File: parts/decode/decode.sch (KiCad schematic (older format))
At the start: 37 parts, among them J1 Conn_02x02_Odd_Even, J10 Conn_01x02, J11 Conn_01x02, J12 Conn_01x02, J13 Conn_01x02, J14 Conn_02x04_Odd_Even, J2 Conn_02x04_Odd_Even, J3 Conn_01x02, J4 Conn_01x02, J5 Conn_01x02, J6 Conn_01x02, J7 Conn_01x02, J8 Conn_01x02, J9 Conn_01x02, K1 HK19F, K10 HK19F, K11 HK19F, K2 HK19F, K3 HK19F, K4 HK19F, K5 HK19F, K6 HK19F, K7 HK19F, K8 HK19F, K9 HK19F

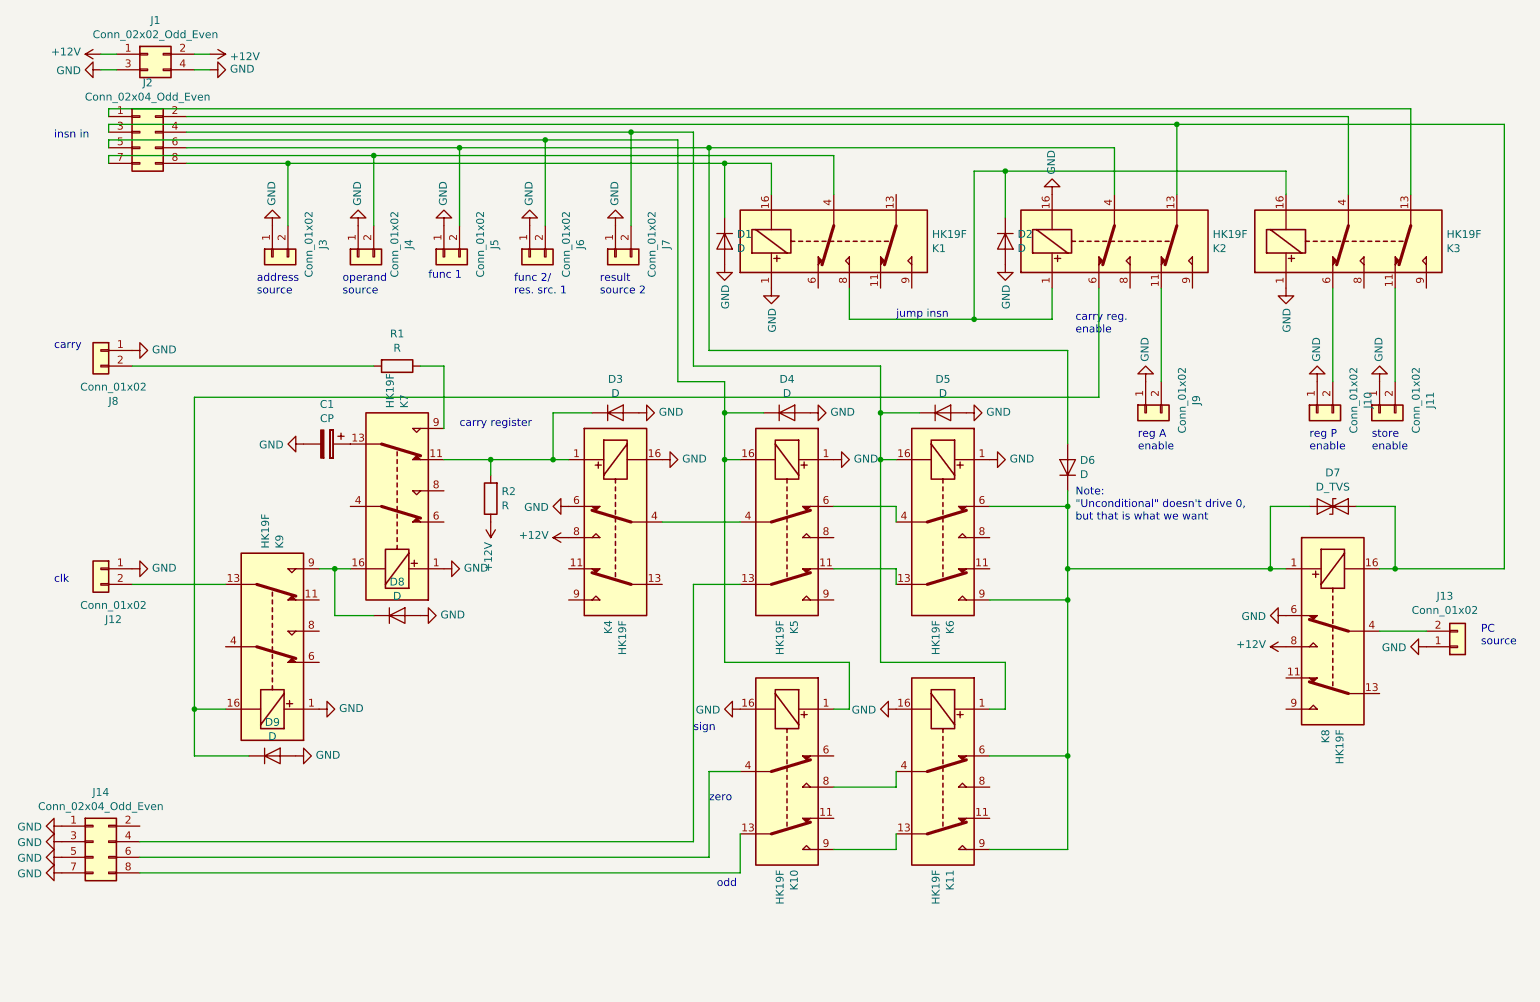
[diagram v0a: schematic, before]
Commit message: Change opcodes (jumps from rediscovered notes).
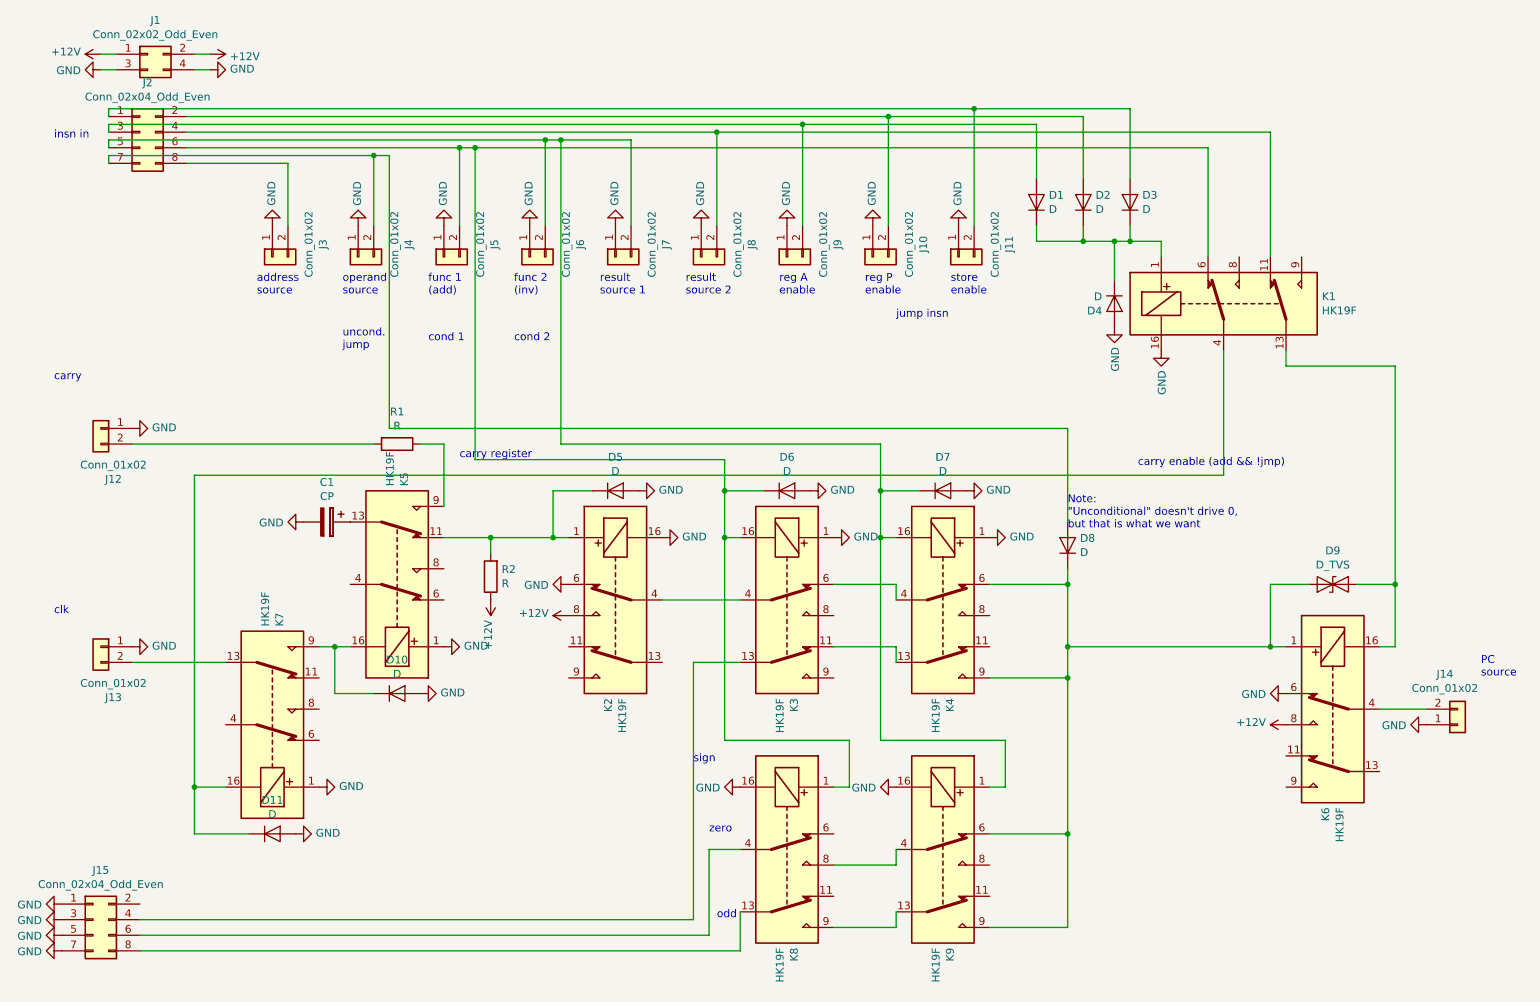
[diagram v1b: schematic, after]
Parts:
- removed K2, K3: HK19F, hk19f:Relay_DPDT_HK19F, symbol hk19f:HK19F
- added D3, D4: D, Diodes_SMD:D_2114, symbol Device:D
- added J7: Conn_01x02, Pin_Headers:Pin_Header_Straight_1x02_Pitch2.54mm, symbol Connector_Generic:Conn_01x02
- renumbered D8 to D10, D9 to D11, D3 to D5, D4 to D6, D5 to D7, D6 to D8, D7 to D9, J8 to J12, J12 to J13, J13 to J14, J14 to J15, J7 to J8, K4 to K2, K5 to K3, K6 to K4, K7 to K5, K8 to K6, K9 to K7, K10 to K8, K11 to K9
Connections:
- net GND: now also K1.16, D4.2 (A), J7.1 (Pin_1); no longer D1.2 (A), D2.2 (A), K1.1
- net at J2.1 (Pin_1): now also J11.2 (Pin_2), D3.2 (A)
- net at J2.2 (Pin_2): now also D2.2 (A), J10.2 (Pin_2)
- net at D9.2 (A2), K6.16: now also K1.13; no longer J2.3 (Pin_3)
- net at D7.1 (K), K4.16, K9.1: now also J2.5 (Pin_5), J6.2 (Pin_2), J7.2 (Pin_2); no longer J2.4 (Pin_4), J8.2 (Pin_2)
- net at D6.1 (K), K3.16, K8.1: now also J2.6 (Pin_6), J5.2 (Pin_2), K1.6; no longer J2.5 (Pin_5), J6.2 (Pin_2)
- net at J2.7 (Pin_7), J4.2 (Pin_2): now also D8.2 (A); no longer K1.4
- net at J2.8 (Pin_8), J3.2 (Pin_2): no longer D1.1 (K), K1.16
- net at K1.11: now also J2.4 (Pin_4), J8.2 (Pin_2)
- net at D2.1 (K): now also D1.1 (K), K1.1, D3.1 (K), D4.1 (K); no longer K1.8
- net at J9.2 (Pin_2): now also D1.2 (A), J2.3 (Pin_3)
- net at D11.1 (K), K7.16: now also K1.4
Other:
- note added: "carry enable (add && !jmp)"
- note added: "cond 1"
- note added: "cond 2"
- note added: "func 1\n(add)"
- note added: "func 2\n(inv)"
- note added: "result\nsource 1"
- note added: "uncond.\njump"
- note removed: "carry reg.\nenable"
- note removed: "func 1"
- note removed: "func 2/\nres. src. 1"
- moved on the sheet: C1, D10, D11, D5, D6, D7, D8, D9, J10, J11, J12, J13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
